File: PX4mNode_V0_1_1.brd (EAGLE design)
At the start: 48.6 x 34.9 mm, 128 parts, among them J201 DF13C-6P-1.25V, J202 DF13C-6P-1.25V, J203 DF13C-6P-1.25V, J301 DF13C-4P-1.25V, J401 DF13C-7P-1.25V, J402 DF13-4P-1.25V, J403 DF13C-4P-1.25V, J404 DF13C-4P-1.25V, J405 DF13C-4P-1.25V, J801 DF13C-3P-1.25V, M3_MOUNT1101 MOUNT-HOLE3.1MM, M3_MOUNT1102 MOUNT-HOLE3.1MM, M3_MOUNT1103 MOUNT-HOLE3.1MM, M3_MOUNT1104 MOUNT-HOLE3.1MM, U101 STM32F4X7VX, U401 MAX3051, U402 MAX3051, X101 3.2x2.5 mm / 24 MHz / 15 ppm

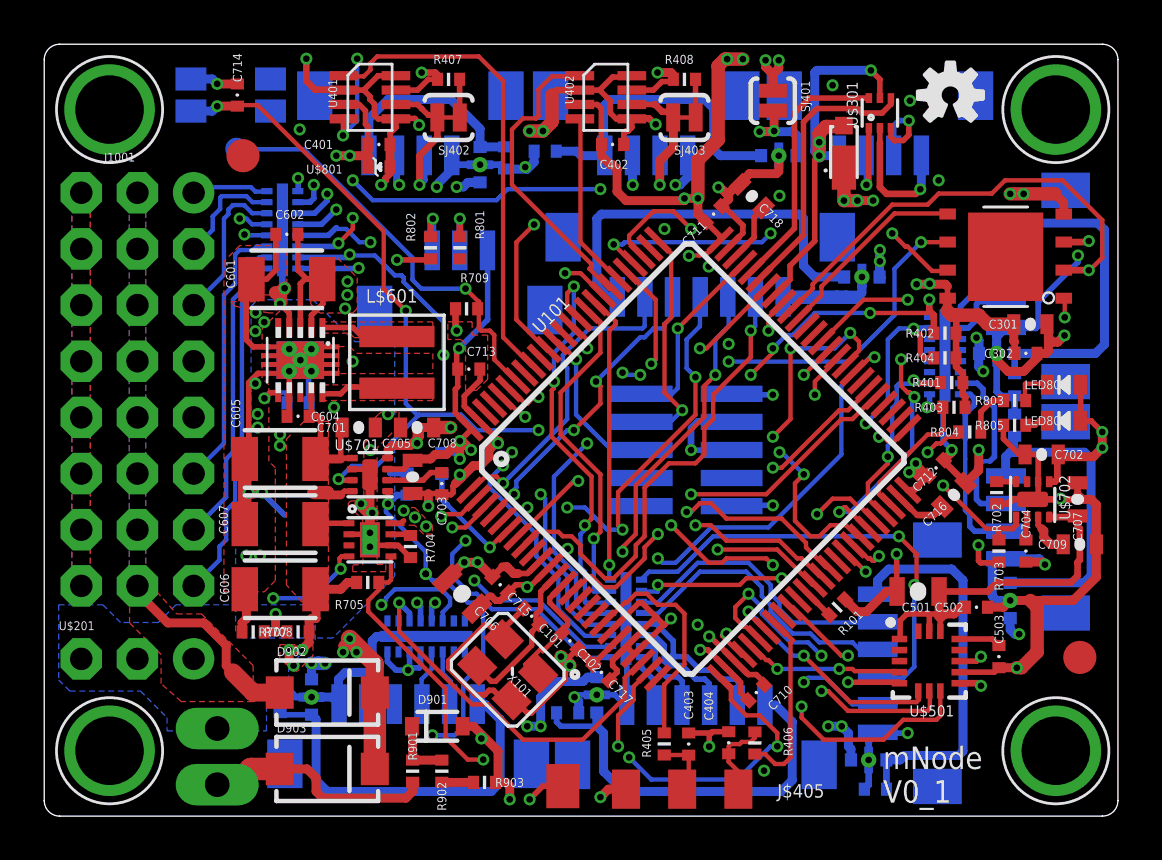
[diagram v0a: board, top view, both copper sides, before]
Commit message: Added SBUS input inverter
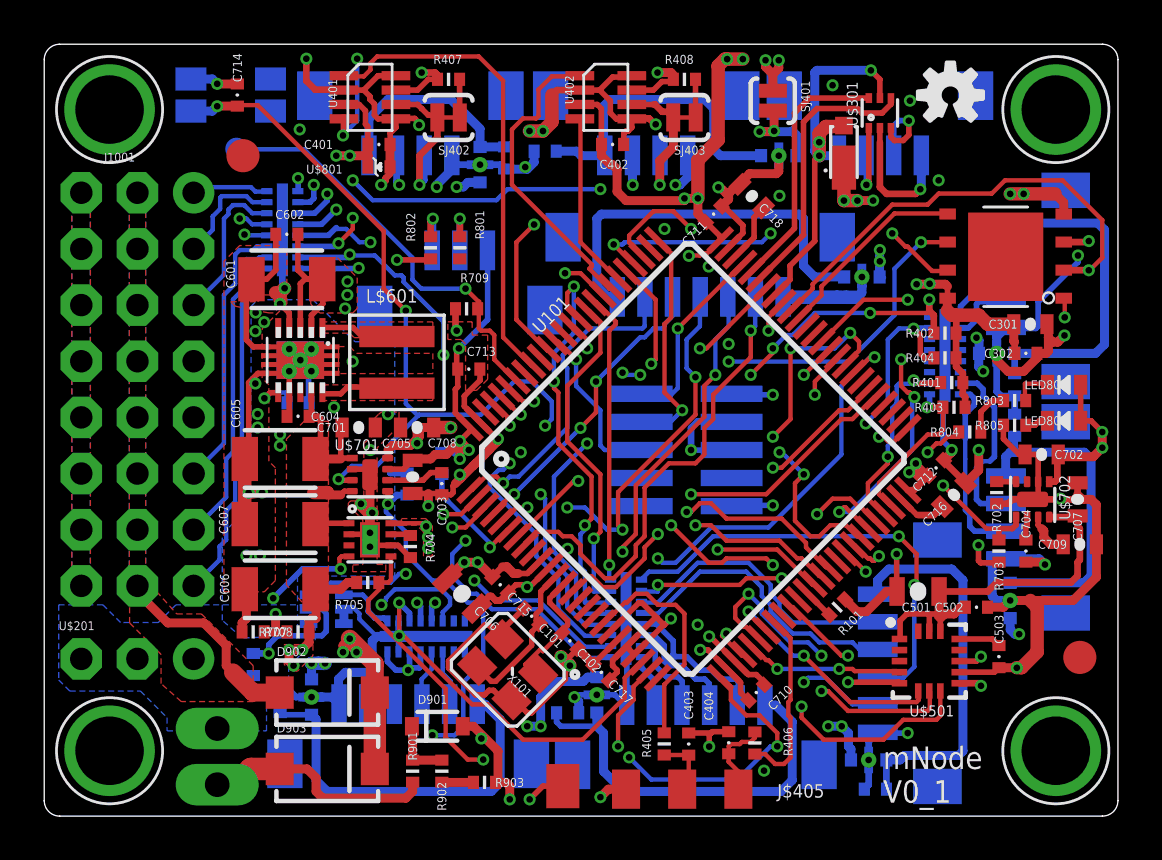
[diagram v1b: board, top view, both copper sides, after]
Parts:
- added C1: 0u1, pixhawk2:0402-CAP
- added U$1: 74LVC2GU04, pixhawk2:SOT363_PHILIPS
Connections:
- removed net PWM_SPARE_OUT: L201.P$1
- new net N$5: L201.P$1, U$1.1
- net FMU-UART8_RX: now also U$1.6
- net FMU-VDD_3V3: now also C1.P$1, U$1.5
- net GND: now also C1.P$2, L201.P$15, L201.P$2, U$1.2, U$1.3
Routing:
- net FMU-VDD_3V3: track 103.3 -> 130.1 mm, vias 21 -> 22
- net FMU-UART8_RX: track 0.00 -> 16.4 mm, vias 0 -> 2
- net GND: track 231.2 -> 234.5 mm, vias 58 -> 59
- net N$5: track 0.00 -> 2.74 mm
- net FMU-!RESET: track 44.8 -> 47.2 mm
- net FMU-CH7: track 34.5 -> 36.8 mm
- net FMU-USART3_RTS: track 39.4 -> 37.4 mm
- net VDD_5V_PERIPH: track 63.2 -> 63.9 mm
- net N$18: track 17.9 -> 17.2 mm
- net VDD_3V3_SPEKTRUM_EN: track 38.4 -> 38.3 mm, vias 6 -> 4

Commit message: Added power selector for PPM/Spektrum/SBUS power output
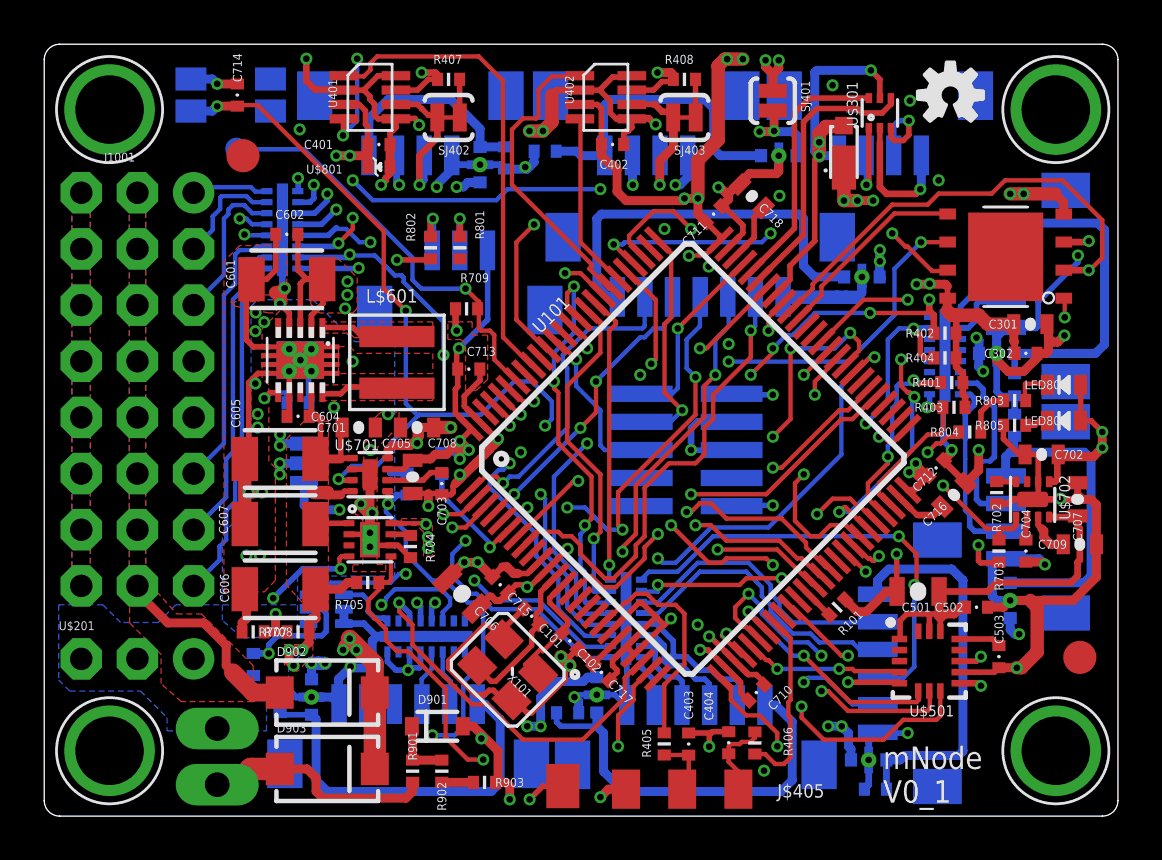
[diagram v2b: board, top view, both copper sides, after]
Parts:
- added JP1: JUMPER-3SMD, SparkFun-Passives:SJ_3
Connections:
- new net VDD_RX_POWER: JP1.2, U$201.2
- net GND: no longer L201.P$15, L201.P$2
- net VDD_3V3_SPEKTRUM: now also JP1.1; no longer U$201.2
- net VDD_5V_PERIPH: now also JP1.3
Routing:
- net VDD_RX_POWER: track 0.00 -> 15.8 mm, vias 0 -> 2
- net VDD_3V3_SPEKTRUM: track 30.3 -> 17.9 mm
- net GND: track 234.5 -> 231.8 mm
- net VDD_5V_PERIPH: track 63.9 -> 66.6 mm, vias 16 -> 17
- net SPEKTRUM_RX: track 34.0 -> 35.3 mm
- net VDD_IN: track 69.1 -> 67.7 mm
- net VDD_3V3_SPEKTRUM_EN: track 38.3 -> 37.5 mm, vias 4 -> 3
- net FMU-CH2: vias 7 -> 5
- added copper zone on layer 15, net V_SERVO

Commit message: Added fiducials to bottom side to support fine pitch packages
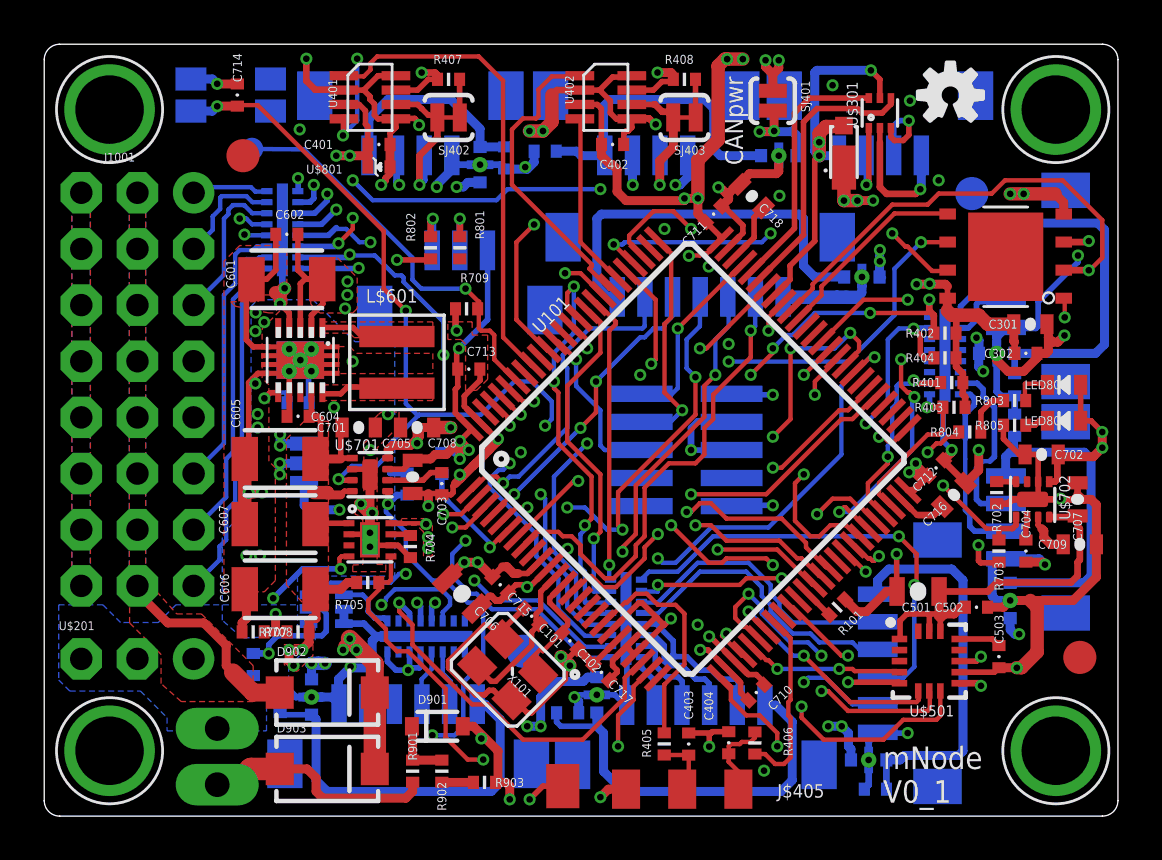
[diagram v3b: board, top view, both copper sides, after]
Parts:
- added JP2, JP3: FIDUCIAL1.5X3, pixhawk2:FIDUCIAL-1.5X3
- moved BOOT 0.70 mm to (18.6, 32.9)
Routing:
- net FMU-BOOT0: track 19.4 -> 18.7 mm
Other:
- board text added: "3V3"
- board text added: "5V"
- board text added: "CANpwr"
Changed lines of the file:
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@@
 <grid distance="0.1" unitdist="mm" unit="mm" style="dots" multiple="1" display="yes" altdistance="4" altunitdist="mil" altunit="mm"/>
 <layers>
-<layer number="1" name="Top" color="4" fill="1" visible="no" active="yes"/>
+<layer number="1" name="Top" color="4" fill="1" visible="yes" active="yes"/>
 <layer number="2" name="Ground" color="2" fill="10" visible="no" active="yes"/>
 <layer number="3" name="Horizontal" color="13" fill="15" visible="no" active="yes"/>
@@
 <layer number="13" name="Route13" color="4" fill="5" visible="no" active="no"/>
 <layer number="14" name="Vertical" color="14" fill="15" visible="no" active="yes"/>
-<layer number="15" name="Power" color="11" fill="15" visible="yes" active="yes"/>
-<layer number="16" name="Bottom" color="1" fill="1" visible="no" active="yes"/>
+<layer number="15" name="Power" color="11" fill="15" visible="no" active="yes"/>
+<layer number="16" name="Bottom" color="1" fill="1" visible="yes" active="yes"/>
 <layer number="17" name="Pads" color="2" fill="1" visible="yes" active="yes"/>
 <layer number="18" name="Vias" color="2" fill="1" visible="yes" active="yes"/>
-<layer number="19" name="Unrouted" color="14" fill="1" visible="yes" active="yes"/>
+<layer number="19" name="Unrouted" color="14" fill="1" visible="no" active="yes"/>
 <layer number="20" name="Dimension" color="15" fill="1" visible="yes" active="yes"/>
-<layer number="21" name="tPlace" color="7" fill="1" visible="no" active="yes"/>
+<layer number="21" name="tPlace" color="7" fill="1" visible="yes" active="yes"/>
 <layer number="22" name="bPlace" color="7" fill="1" visible="yes" active="yes"/>
-<layer number="23" name="tOrigins" color="15" fill="1" visible="no" active="yes"/>
+<layer number="23" name="tOrigins" color="15" fill="1" visible="yes" active="yes"/>
 <layer number="24" name="bOrigins" color="15" fill="1" visible="yes" active="yes"/>
 <layer number="25" name="tNames" color="7" fill="1" visible="no" active="yes"/>
@@
 <layer number="37" name="tTest" color="7" fill="1" visible="no" active="yes"/>
 <layer number="38" name="bTest" color="7" fill="1" visible="no" active="yes"/>
-<layer number="39" name="tKeepout" color="4" fill="11" visible="no" active="yes"/>
+<layer number="39" name="tKeepout" color="4" fill="11" visible="yes" active="yes"/>
 <layer number="40" name="bKeepout" color="1" fill="11" visible="yes" active="yes"/>
-<layer number="41" name="tRestrict" color="4" fill="10" visible="no" active="yes"/>
+<layer number="41" name="tRestrict" color="4" fill="10" visible="yes" active="yes"/>
 <layer number="42" name="bRestrict" color="1" fill="10" visible="yes" active="yes"/>
 <layer number="43" name="vRestrict" color="2" fill="10" visible="no" active="yes"/>
@@
 <layer number="49" name="Reference" color="7" fill="1" visible="no" active="yes"/>
 <layer number="50" name="dxf" color="7" fill="1" visible="no" active="yes"/>
-<layer number="51" name="tDocu" color="7" fill="1" visible="no" active="yes"/>
+<layer number="51" name="tDocu" color="7" fill="1" visible="yes" active="yes"/>
 <layer number="52" name="bDocu" color="7" fill="1" visible="yes" active="yes"/>
 <layer number="53" name="tGND_GNDA" color="7" fill="9" visible="no" active="no"/>
@@
 <text x="26.1112" y="23.0632" size="0.762" layer="22" font="vector" ratio="15" rot="MR180">SAFETY</text>
 <text x="54.356" y="10.668" size="0.762" layer="22" font="vector" ratio="15" rot="MR180">I2C2</text>
-<text x="19.2024" y="33.3232" size="0.762" layer="22" font="vector" ratio="15" rot="MR180">CAN2</text>
+<text x="19.4024" y="33.3232" size="0.762" layer="22" font="vector" ratio="15" rot="MR180">CAN2</text>
 <wire x1="9.245" y1="3.425" x2="9.245" y2="36.95" width="0" layer="20"/>
+<text x="22.2112" y="20.5632" size="0.762" layer="22" font="vector" ratio="15" rot="MR180">3V3</text>
+<text x="19.1112" y="17.0632" size="0.762" layer="22" font="vector" ratio="15" rot="MR180">5V</text>
+<text x="40.8504" y="32.1848" size="0.8128" layer="21" font="vector" ratio="15" rot="R90">CANpwr</text>
 </plain>
 <attributes>
@@
 <attribute name="PARTNO" value="ERA-2AEB103X" x="18.6944" y="11.0744" size="1.778" layer="27" rot="R180" display="off"/>
 </element>
-<element name="BOOT" library="pixhawk2" package="PAD.04X.04" value="PAD.04" x="17.9416" y="32.9184" smashed="yes" rot="MR0">
-<attribute name="PARTNO" value="*" x="18.348" y="32.9184" size="1.778" layer="28" rot="MR0" display="off"/>
-<attribute name="BOM" value="EXCLUDE" x="18.348" y="32.9184" size="1.778" layer="28" rot="MR0" display="off"/>
-<attribute name="NAME" x="15.1392" y="33.1556" size="0.5" layer="22" font="vector" ratio="15" rot="MR180"/>
+<element name="BOOT" library="pixhawk2" package="PAD.04X.04" value="PAD.04" x="18.6416" y="32.9184" smashed="yes" rot="MR0">
+<attribute name="PARTNO" value="*" x="19.048" y="32.9184" size="1.778" layer="28" rot="MR0" display="off"/>
+<attribute name="BOM" value="EXCLUDE" x="19.048" y="32.9184" size="1.778" layer="28" rot="MR0" display="off"/>
+<attribute name="NAME" x="17.8392" y="32.0556" size="0.5" layer="22" font="vector" ratio="15" rot="MR180"/>
 </element>
 <element name="J301" library="con-hirose-df13" package="DF13C-4P-1.25V" value="DF13C-4P-1.25V" x="47.0408" y="33.528" locked="yes" rot="MR180">
@@
 </element>
 <element name="JP1" library="SparkFun-Passives" package="SJ_3" value="JUMPER-3SMD" x="21" y="18.7" rot="MR270"/>
+<element name="JP2" library="pixhawk2" package="FIDUCIAL-1.5X3" value="FIDUCIAL1.5X3" x="51.2" y="30.9" rot="MR0">
+<attribute name="PARTNO" value="*" x="51.2" y="30.9" size="1.778" layer="28" rot="MR0" display="off"/>
+<attribute name="BOM" value="EXCLUDE" x="51.2" y="30.9" size="1.778" layer="28" rot="MR0" display="off"/>
+</element>
+<element name="JP3" library="pixhawk2" package="FIDUCIAL-1.5X3" value="FIDUCIAL1.5X3" x="30.9" y="10.2" rot="MR0">
+<attribute name="PARTNO" value="*" x="30.9" y="10.2" size="1.778" layer="28" rot="MR0" display="off"/>
+<attribute name="BOM" value="EXCLUDE" x="30.9" y="10.2" size="1.778" layer="28" rot="MR0" display="off"/>
+</element>
 </elements>
 <signals>
@@
 <wire x1="30.6" y1="22.4" x2="29.6" y2="23.4" width="0.2" layer="1"/>
 <wire x1="30.6" y1="22.4" x2="30.626625" y2="22.43313125" width="0.2" layer="1"/>
-<wire x1="21" y1="32.9" x2="18" y2="32.9" width="0.2" layer="16"/>
+<wire x1="21" y1="32.9" x2="20.9" y2="32.9" width="0.2" layer="16"/>
 <wire x1="25.9" y1="28" x2="21" y2="32.9" width="0.2" layer="16"/>
 <wire x1="25.9" y1="27" x2="25.9" y2="28" width="0.2" layer="16"/>
@@
 <wire x1="28.9" y1="26" x2="28.3" y2="26.6" width="0.2" layer="1"/>
 <wire x1="28.9" y1="24.8" x2="28.9" y2="26" width="0.2" layer="1"/>
-<wire x1="18" y1="32.9" x2="17.9416" y2="32.9184" width="0.2" layer="16"/>
+<wire x1="20.9" y1="32.9" x2="18.6416" y2="32.9184" width="0.2" layer="16"/>
 <via x="28.3" y="26.6" extent="1-16" drill="0.3" diameter="0.55"/>
 <wire x1="28.9" y1="26" x2="28.9" y2="25.6408" width="0.254" layer="1"/>

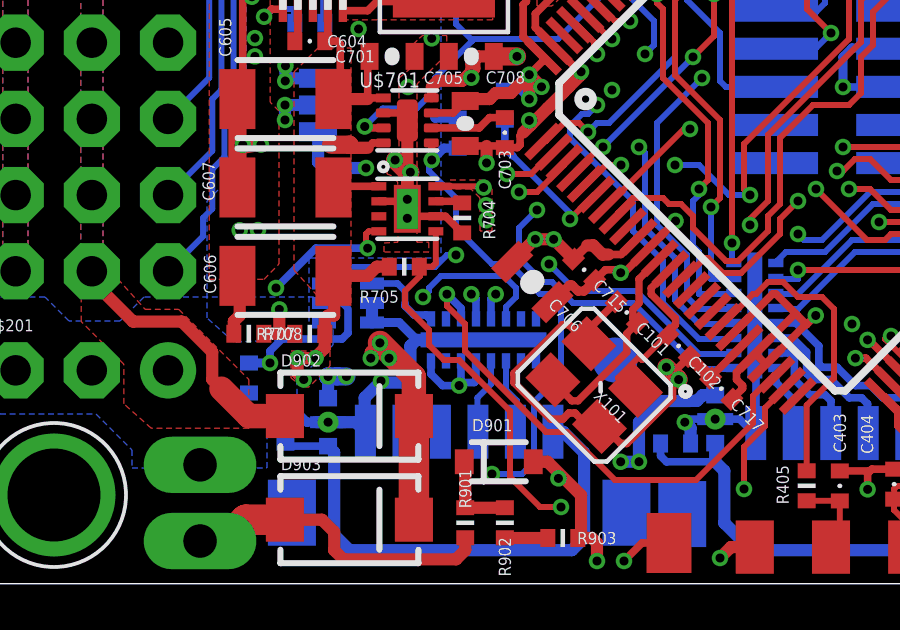
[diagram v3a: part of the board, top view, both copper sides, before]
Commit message: Reworked sbus input to make space for sbus output
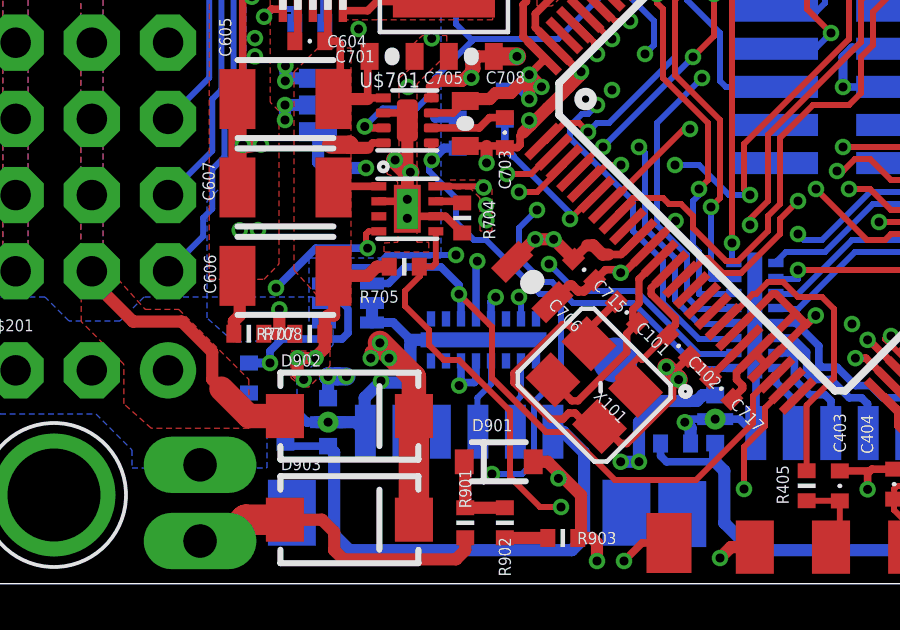
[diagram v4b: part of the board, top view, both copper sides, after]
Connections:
- removed net N$5: L201.P$1, U$1.1
- net FMU-UART7_TX: now also L201.P$7; no longer L201.P$6
- net N$18: no longer L201.P$16
- net PPM_INPUT: now also U$1.1
- net SERIAL3_TX: now also L201.P$10; no longer L201.P$11
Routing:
- net FMU-UART7_TX: track 30.9 -> 24.1 mm
- net PPM_INPUT: track 17.3 -> 20.6 mm
- net N$5: track 2.74 -> 0.00 mm
- net N$18: track 17.2 -> 15.7 mm
- net SPEKTRUM_RX: track 35.3 -> 36.5 mm
